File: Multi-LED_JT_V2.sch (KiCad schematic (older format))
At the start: 11 parts, among them Q1 BC817-25, SW1 SW_DPDT

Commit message: associated wrong footprint
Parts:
- SW1: footprint lib_fp:SPDT_OS102011MA1QN1 -> lib_fp:DPDT_JS202011JAQN
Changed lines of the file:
@@
 F 0 "SW1" H 2750 4970 50  0000 C CNN
 F 1 "SW_DPDT" H 2750 4600 50  0000 C CNN
-F 2 "lib_fp:SPDT_OS102011MA1QN1" H 2750 4800 50  0001 C CNN
+F 2 "lib_fp:DPDT_JS202011JAQN" H 2750 4800 50  0001 C CNN
 F 3 "" H 2750 4800 50  0001 C CNN
 F 4 "CK" H 2750 4800 60  0001 C CNN "Manufacture"

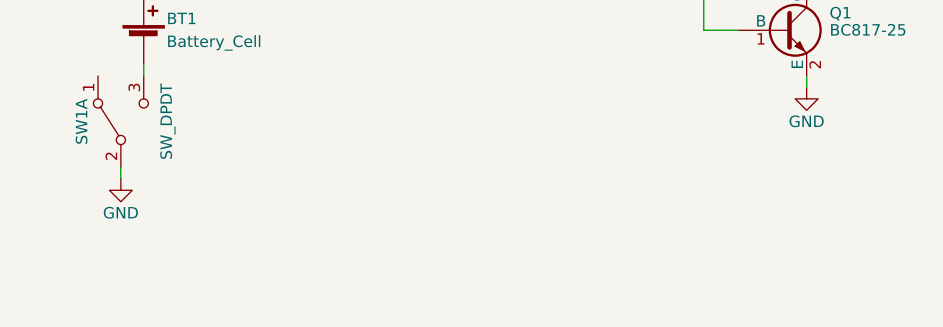
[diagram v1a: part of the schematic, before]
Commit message: JS202011JCQN is out of stock, JS102011JAQN is replacment
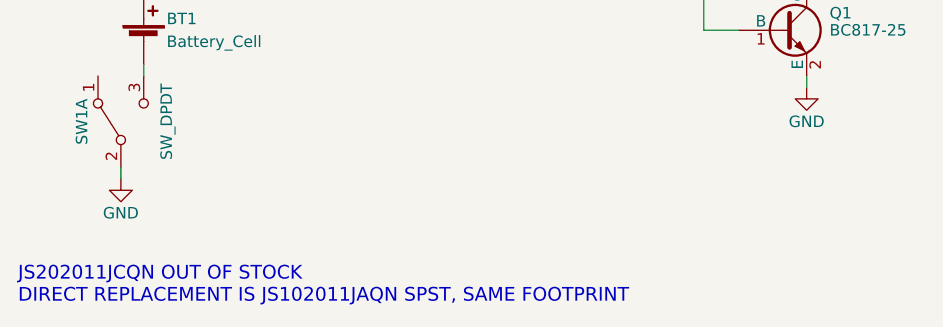
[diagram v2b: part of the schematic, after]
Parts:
- SW1: Description SWITCH SLIDE DPDT 300MA 6V -> SWITCH SLIDE SPDT 300MA 6V; Mfg Part Number JS202011JAQN -> JS102011JAQN
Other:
- note added: "JS202011JCQN OUT OF STOCK\nDIRECT REPLACEMENT IS JS102011JAQN SPST, SAME FOOTPRINT"
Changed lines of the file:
@@
 F 3 "" H 2750 4800 50  0001 C CNN
 F 4 "CK" H 2750 4800 60  0001 C CNN "Manufacture"
-F 5 "JS202011JAQN" H 2750 4800 60  0001 C CNN "Mfg Part Number"
+F 5 "JS102011JAQN" H 2750 4800 60  0001 C CNN "Mfg Part Number"
 F 6 "SMD" H 2750 4800 60  0001 C CNN "Package"
-F 7 "SWITCH SLIDE DPDT 300MA 6V" H 2750 4800 60  0001 C CNN "Description"
+F 7 "SWITCH SLIDE SPDT 300MA 6V" H 2750 4800 60  0001 C CNN "Description"
 	1    2750 4800
 	0    -1   -1   0
@@
 Wire Wire Line
 	2750 5050 2750 5000
+Text Notes 2300 5600 0    60   ~ 0
+JS202011JCQN OUT OF STOCK\nDIRECT REPLACEMENT IS JS102011JAQN SPST, SAME FOOTPRINT
 $EndSCHEMATC
